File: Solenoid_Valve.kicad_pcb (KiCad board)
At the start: 2 copper layers, 84.3 x 41.6 mm, 60 parts, among them IC1 Si8621AB-B-ISR, J1 Conn_01x02, J10 Conn_01x05, J11 Conn_01x02, J12 Conn_01x02, J13 Conn_01x02, J14 Conn_01x02, J15 Conn_01x02, J16 Conn_01x02, J17 Conn_01x02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

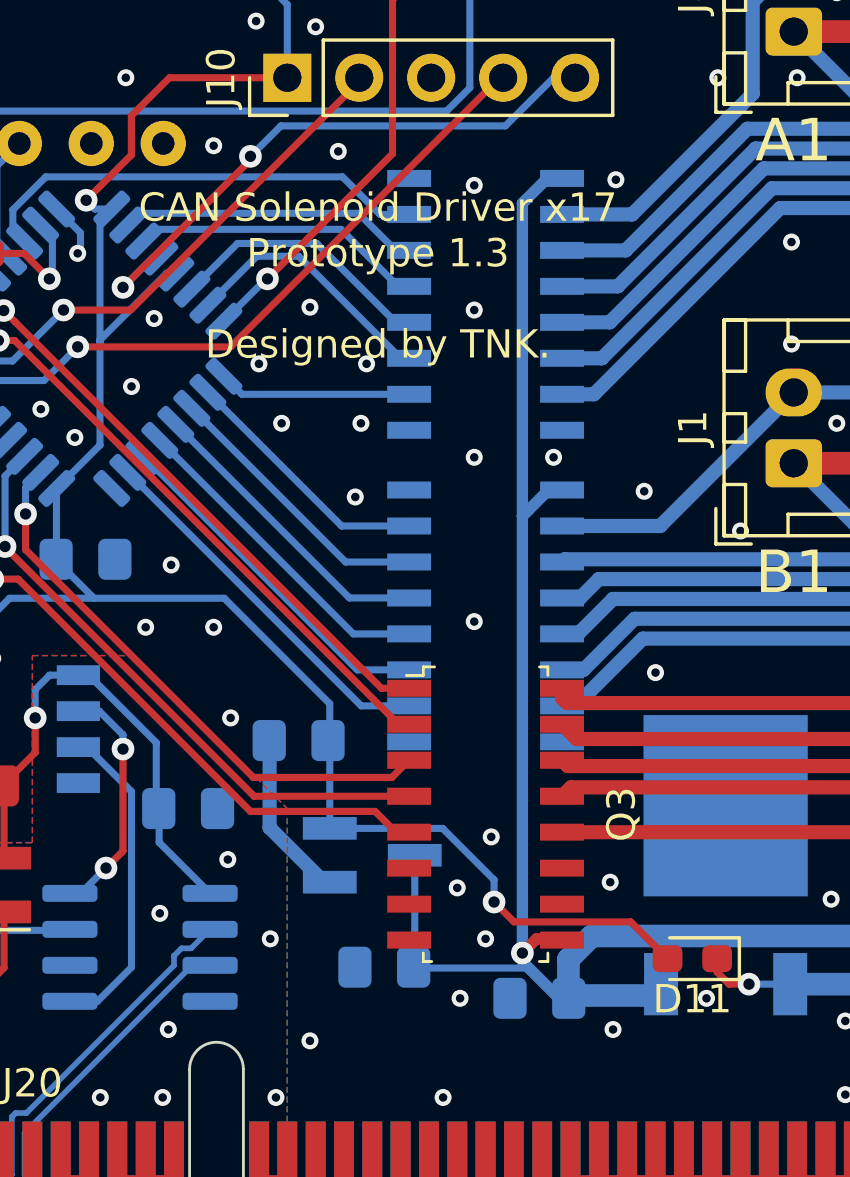
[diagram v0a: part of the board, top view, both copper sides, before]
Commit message: Fix: Symbol & Footprint Library
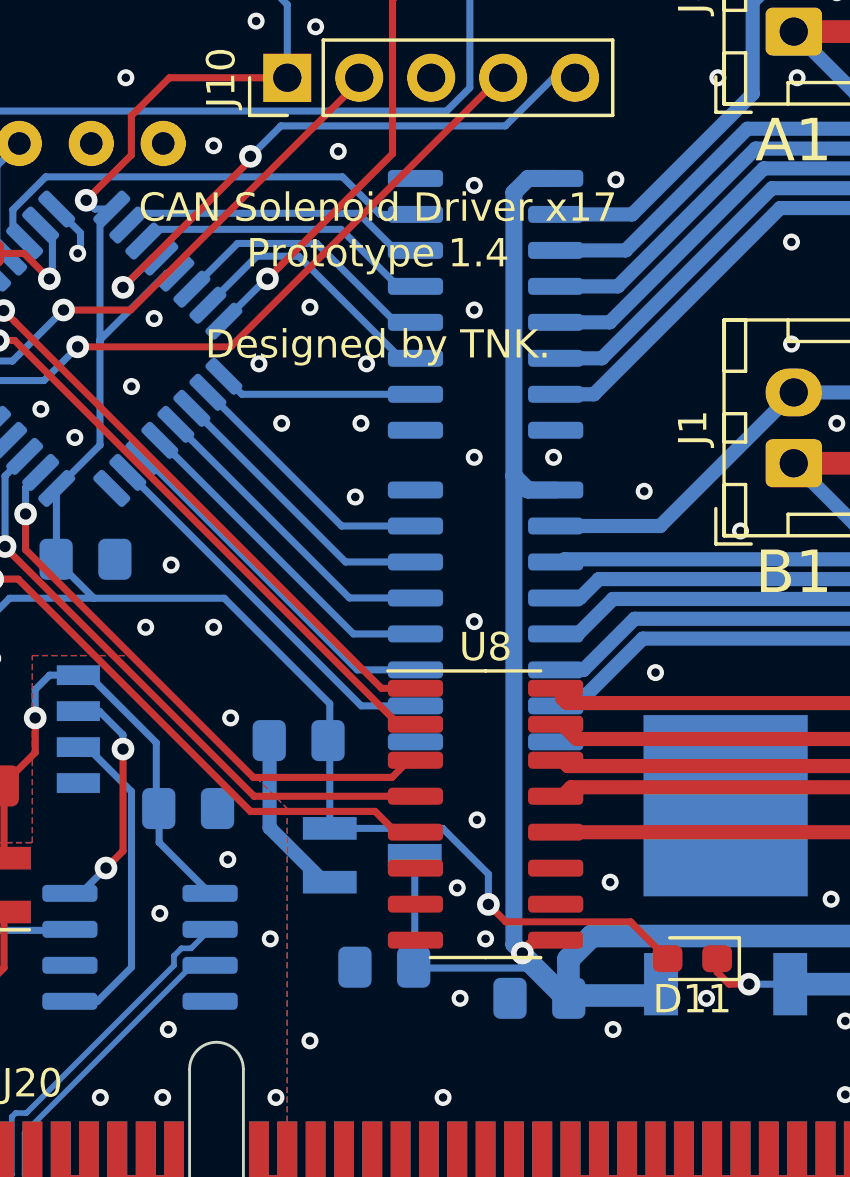
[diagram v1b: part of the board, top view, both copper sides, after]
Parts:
- removed Q1, Q2, Q3: ULN2004D1013TR, digikey-footprints:SOIC-16_W3.90mm
- added U6: ULN2004, Package_SO:SOIC-16_3.9x9.9mm_P1.27mm, B.Cu at (172.0, 115.0)
- added U7: ULN2004, Package_SO:SOIC-16_3.9x9.9mm_P1.27mm, B.Cu at (172.0, 126.0)
- added U8: ULN2004, Package_SO:SOIC-16_3.9x9.9mm_P1.27mm, F.Cu at (172.0, 133.0)
- U3: value STM32F042K6Tx -> STM32F303K8Tx
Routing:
- net +12V: track 305.1 -> 308.5 mm
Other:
- board text added: "CAN Solenoid Driver x17 Prototype 1.4 Designed by TNK."
- board text removed: "CAN Solenoid Driver x17 Prototype 1.3 Designed by TNK."

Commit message: Update: ダーリントントランジスタアレイをULN2003に変更
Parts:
- U6, U7, U8: value ULN2004 -> ULN2003
